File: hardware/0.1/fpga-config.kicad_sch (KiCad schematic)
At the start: 31 parts, among them J2 JTAG, J5 USB_C_Receptacle_USB2.0, Q1 BSS138, SW1 KMR2, U1 ECP5U_12_CABGA256, U4 USBLC6-2SC6, U6 W25Q128JVSIQ

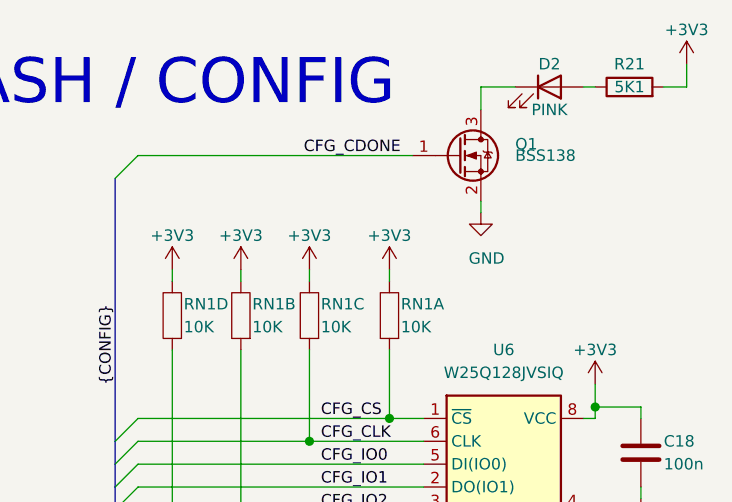
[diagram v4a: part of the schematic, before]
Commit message: change LEDs, optimise parts
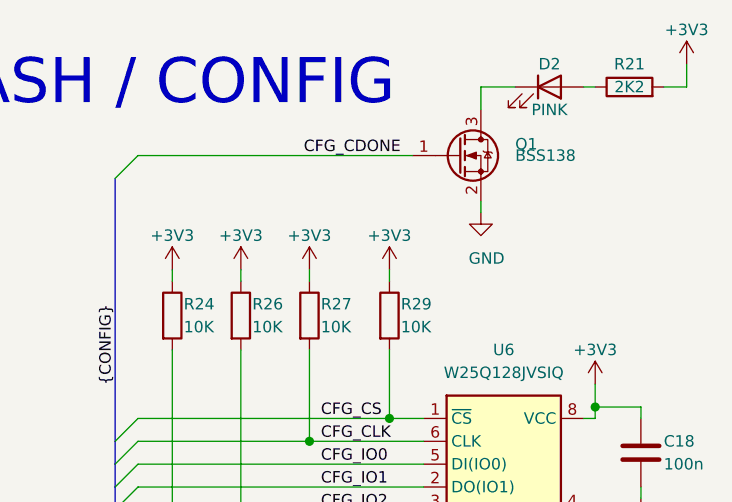
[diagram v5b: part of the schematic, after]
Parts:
- removed RN1: 10K, Resistor_SMD:R_Array_Convex_4x0402, symbol josh-passive:RN
- added R24, R26, R27, R29: 10K, Resistor_SMD:R_0402_1005Metric, symbol Device:R
- J5: footprint josh-connectors:USB_C_U262-161N-4BVC11 -> josh-connectors:USB_C_Receptacle_HRO_TYPE-C-31-M-12
- Q1: LCSC (none) -> C193366; MPN (none) -> BSS138PW,115
- R21: value 5K1 -> 2K2
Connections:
- net +3V3: now also R24.1, R26.1, R27.1, R29.1
- net CFG_CLK: now also R27.2
- net CFG_CS: now also R29.2
- net CFG_IO2: now also R26.2
- net CFG_IO3: now also R24.2
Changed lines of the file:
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@@
   (junction (at 269.24 57.15) (diameter 1.016) (color 0 0 0 0))
   (junction (at 269.24 71.12) (diameter 1.016) (color 0 0 0 0))
+  (no_connect (at 46.355 66.04))
+  (no_connect (at 229.87 137.16))
+  (no_connect (at 229.87 116.84))
+  (no_connect (at 229.87 111.76))
+  (no_connect (at 229.87 119.38))
+  (no_connect (at 229.87 144.78))
   (no_connect (at 229.87 121.92))
-  (no_connect (at 229.87 111.76))
-  (no_connect (at 229.87 144.78))
   (no_connect (at 46.355 63.5))
   (no_connect (at 229.87 114.3))
-  (no_connect (at 229.87 119.38))
-  (no_connect (at 229.87 116.84))
-  (no_connect (at 46.355 66.04))
-  (no_connect (at 229.87 137.16))
   (bus_entry (at 114.935 49.53) (size 2.54 -2.54)
     (stroke (width 0.1524) (type solid) (color 0 0 0 0))
@@
     (property "DNP" "" (id 4) (at 179.07 114.3 0)
       (effects (font (size 1.27 1.27)) (justify left bottom))
-    )
-  )
-  (symbol (lib_id "josh-passive:RN") (at 222.25 46.99 90) (unit 4)
-    (in_bom yes) (on_board yes)
-    (property "Reference" "RN1" (id 0) (at 223.52 45.72 90)
-      (effects (font (size 1.27 1.27)) (justify right))
-    )
-    (property "Value" "10K" (id 1) (at 223.52 48.26 90)
-      (effects (font (size 1.27 1.27)) (justify right))
-    )
-    (property "Footprint" "Resistor_SMD:R_Array_Convex_4x0402" (id 2) (at 222.25 46.99 90)
-      (effects (font (size 1.27 1.27)) hide)
-    )
-    (property "Datasheet" "~" (id 3) (at 222.25 46.99 90)
-      (effects (font (size 1.27 1.27)) hide)
-    )
-  )
-  (symbol (lib_id "josh-passive:RN") (at 229.87 46.99 90) (unit 2)
-    (in_bom yes) (on_board yes)
-    (property "Reference" "RN1" (id 0) (at 231.14 45.72 90)
-      (effects (font (size 1.27 1.27)) (justify right))
-    )
-    (property "Value" "10K" (id 1) (at 231.14 48.26 90)
-      (effects (font (size 1.27 1.27)) (justify right))
-    )
-    (property "Footprint" "Resistor_SMD:R_Array_Convex_4x0402" (id 2) (at 229.87 46.99 90)
-      (effects (font (size 1.27 1.27)) hide)
-    )
-    (property "Datasheet" "~" (id 3) (at 229.87 46.99 90)
-      (effects (font (size 1.27 1.27)) hide)
-    )
-  )
-  (symbol (lib_id "josh-passive:RN") (at 237.49 46.99 90) (unit 3)
-    (in_bom yes) (on_board yes)
-    (property "Reference" "RN1" (id 0) (at 238.76 45.72 90)
-      (effects (font (size 1.27 1.27)) (justify right))
-    )
-    (property "Value" "10K" (id 1) (at 238.76 48.26 90)
-      (effects (font (size 1.27 1.27)) (justify right))
-    )
-    (property "Footprint" "Resistor_SMD:R_Array_Convex_4x0402" (id 2) (at 237.49 46.99 90)
-      (effects (font (size 1.27 1.27)) hide)
-    )
-    (property "Datasheet" "~" (id 3) (at 237.49 46.99 90)
-      (effects (font (size 1.27 1.27)) hide)
-    )
-  )
-  (symbol (lib_id "josh-passive:RN") (at 246.38 46.99 90) (unit 1)
-    (in_bom yes) (on_board yes)
-    (property "Reference" "RN1" (id 0) (at 247.65 45.72 90)
-      (effects (font (size 1.27 1.27)) (justify right))
-    )
-    (property "Value" "10K" (id 1) (at 247.65 48.26 90)
-      (effects (font (size 1.27 1.27)) (justify right))
-    )
-    (property "Footprint" "Resistor_SMD:R_Array_Convex_4x0402" (id 2) (at 246.38 46.99 90)
-      (effects (font (size 1.27 1.27)) hide)
-    )
-    (property "Datasheet" "~" (id 3) (at 246.38 46.99 90)
-      (effects (font (size 1.27 1.27)) hide)
     )
   )
@@
     (property "DNP" "DNP" (id 4) (at 212.09 144.78 90))
   )
+  (symbol (lib_id "Device:R") (at 222.25 46.99 0) (unit 1)
+    (in_bom yes) (on_board yes)
+    (property "Reference" "R24" (id 0) (at 223.52 45.72 0)
+      (effects (font (size 1.27 1.27)) (justify left))
+    )
+    (property "Value" "10K" (id 1) (at 223.52 48.26 0)
+      (effects (font (size 1.27 1.27)) (justify left))
+    )
+    (property "Footprint" "Resistor_SMD:R_0402_1005Metric" (id 2) (at 220.472 46.99 90)
+      (effects (font (size 1.27 1.27)) hide)
+    )
+    (property "Datasheet" "~" (id 3) (at 222.25 46.99 0)
+      (effects (font (size 1.27 1.27)) hide)
+    )
+  )
+  (symbol (lib_id "Device:R") (at 229.87 46.99 0) (unit 1)
+    (in_bom yes) (on_board yes)
+    (property "Reference" "R26" (id 0) (at 231.14 45.72 0)
+      (effects (font (size 1.27 1.27)) (justify left))
+    )
+    (property "Value" "10K" (id 1) (at 231.14 48.26 0)
+      (effects (font (size 1.27 1.27)) (justify left))
+    )
+    (property "Footprint" "Resistor_SMD:R_0402_1005Metric" (id 2) (at 228.092 46.99 90)
+      (effects (font (size 1.27 1.27)) hide)
+    )
+    (property "Datasheet" "~" (id 3) (at 229.87 46.99 0)
+      (effects (font (size 1.27 1.27)) hide)
+    )
+  )
+  (symbol (lib_id "Device:R") (at 237.49 46.99 0) (unit 1)
+    (in_bom yes) (on_board yes)
+    (property "Reference" "R27" (id 0) (at 238.76 45.72 0)
+      (effects (font (size 1.27 1.27)) (justify left))
+    )
+    (property "Value" "10K" (id 1) (at 238.76 48.26 0)
+      (effects (font (size 1.27 1.27)) (justify left))
+    )
+    (property "Footprint" "Resistor_SMD:R_0402_1005Metric" (id 2) (at 235.712 46.99 90)
+      (effects (font (size 1.27 1.27)) hide)
+    )
+    (property "Datasheet" "~" (id 3) (at 237.49 46.99 0)
+      (effects (font (size 1.27 1.27)) hide)
+    )
+  )
+  (symbol (lib_id "Device:R") (at 246.38 46.99 0) (unit 1)
+    (in_bom yes) (on_board yes)
+    (property "Reference" "R29" (id 0) (at 247.65 45.72 0)
+      (effects (font (size 1.27 1.27)) (justify left))
+    )
+    (property "Value" "10K" (id 1) (at 247.65 48.26 0)
+      (effects (font (size 1.27 1.27)) (justify left))
+    )
+    (property "Footprint" "Resistor_SMD:R_0402_1005Metric" (id 2) (at 244.602 46.99 90)
+      (effects (font (size 1.27 1.27)) hide)
+    )
+    (property "Datasheet" "~" (id 3) (at 246.38 46.99 0)
+      (effects (font (size 1.27 1.27)) hide)
+    )
+  )
   (symbol (lib_id "Device:R") (at 273.05 21.59 90) (unit 1)
     (in_bom yes) (on_board yes)
     (property "Reference" "R21" (id 0) (at 273.05 19.05 90))
-    (property "Value" "5K1" (id 1) (at 273.05 21.59 90))
+    (property "Value" "2K2" (id 1) (at 273.05 21.59 90))
     (property "Footprint" "Resistor_SMD:R_0402_1005Metric" (id 2) (at 273.05 23.368 90)
       (effects (font (size 1.27 1.27)) hide)
@@
       (effects (font (size 1.27 1.27)) (justify left) hide)
     )
+    (property "LCSC" "C193366" (id 4) (at 254 29.21 0)
+      (effects (font (size 1.27 1.27)) hide)
+    )
+    (property "MPN" "BSS138PW,115" (id 5) (at 254 29.21 0)
+      (effects (font (size 1.27 1.27)) hide)
+    )
   )
   (symbol (lib_id "josh-ic:ECP5U_12_CABGA256") (at 78.74 104.14 0) (unit 9)
@@
     (property "Reference" "J5" (id 0) (at 22.225 29.21 0))
     (property "Value" "USB_C_Receptacle_USB2.0" (id 1) (at 33.655 31.75 0))
-    (property "Footprint" "josh-connectors:USB_C_U262-161N-4BVC11" (id 2) (at 34.925 50.8 0)
-      (effects (font (size 1.27 1.27)) hide)
-    )
+    (property "Footprint" "josh-connectors:USB_C_Receptacle_HRO_TYPE-C-31-M-12" (id 2) (at 34.925 50.8 0)
+      (effects (font (size 1.27 1.27)) hide)
+    )

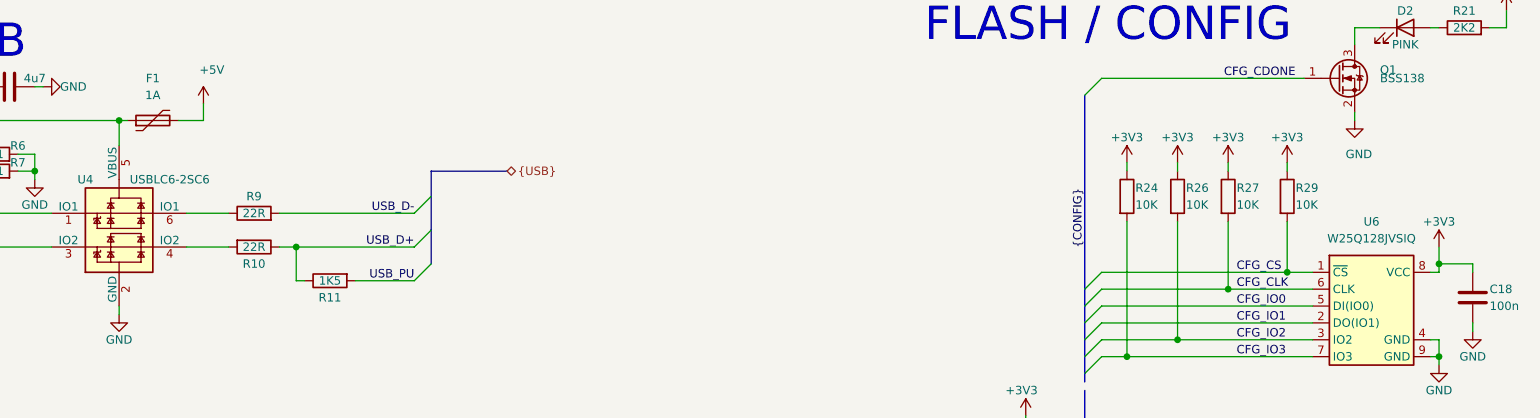
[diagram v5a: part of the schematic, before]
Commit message: add part numbers
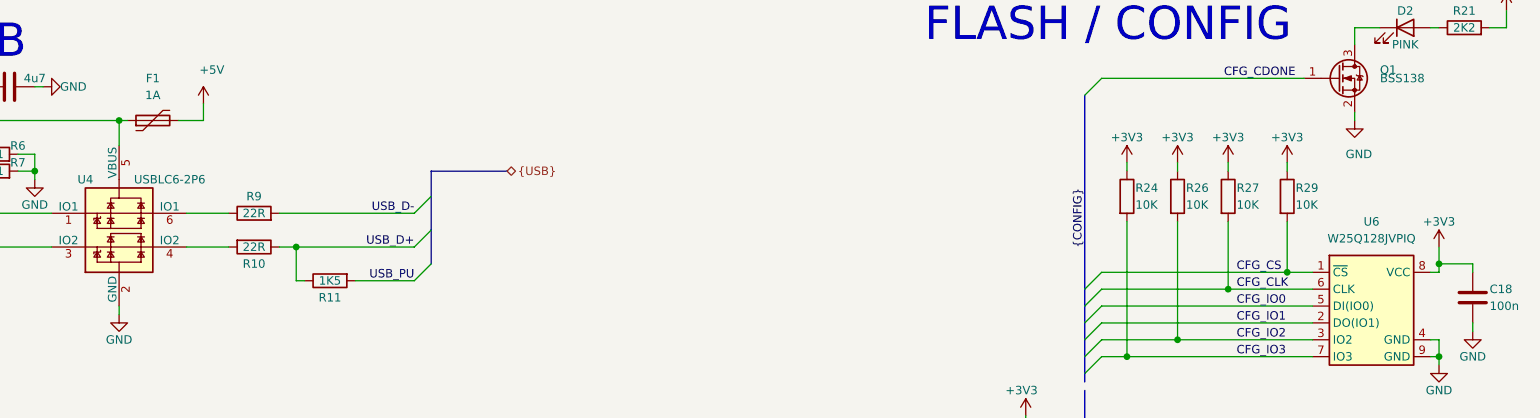
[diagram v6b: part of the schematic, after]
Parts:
- C13, C15, C17, C18: LCSC (none) -> C1525; MPN (none) -> CL05B104KO5NNNC; Manufacturer (none) -> Samsung Electro-Mechanics
- C6: LCSC (none) -> C19666; MPN (none) -> CL10A475KO8NNNC; Manufacturer (none) -> Samsung Electro-Mechanics
- D2: LCSC (none) -> C268294; MPN (none) -> OSK40603C1E; Manufacturer (none) -> OptoSupply
- F1: LCSC (none) -> C207017; MPN (none) -> 0603L100SLYR; Manufacturer (none) -> Littelfuse
- J5: LCSC (none) -> C165948; MPN (none) -> TYPE-C-31-M-12; Manufacturer (none) -> Korean Hroparts Elec
- Q1: Manufacturer (none) -> Nexperia
- R10, R20, R9: LCSC (none) -> C25152; MPN (none) -> 0402WGJ0220TCE; Manufacturer (none) -> UNI-ROYAL(Uniroyal Elec)
- R11, R13, R14, R15, R16, R17, R18: LCSC (none) -> C25867; MPN (none) -> 0402WGF1501TCE; Manufacturer (none) -> UNI-ROYAL(Uniroyal Elec)
- R12, R19, R6, R7: LCSC (none) -> C25905; MPN (none) -> 0402WGF5101TCE; Manufacturer (none) -> UNI-ROYAL(Uniroyal Elec)
- R21: LCSC (none) -> C25933; MPN (none) -> 0402WGJ0222TCE; Manufacturer (none) -> UNI-ROYAL(Uniroyal Elec)
- R24, R26, R27, R29, R8: LCSC (none) -> C25531; MPN (none) -> 0402WGJ0103TCE; Manufacturer (none) -> UNI-ROYAL(Uniroyal Elec)
- SW1: LCSC (none) -> C318893; MPN (none) -> TS-1185EC-C-D-B; Manufacturer (none) -> XKB Connectivity
- U1: MPN (none) -> LFE5U-12F-8BG256C; Manufacturer (none) -> Lattice; Mouser (none) -> 842-LFE5U12F8BG256C
- U4: value USBLC6-2SC6 -> USBLC6-2P6; LCSC (none) -> C15999; MPN (none) -> USBLC6-2P6; Manufacturer (none) -> STMicroelectronics
- U6: value W25Q128JVSIQ -> W25Q128JVPIQ; MPN (none) -> W25Q128JVPIM; Manufacturer (none) -> Winbond; Mouser (none) -> 454-W25Q128JVPIM

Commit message: design review done
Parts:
- U1: MPN LFE5U-12F-8BG256C -> LFE5U12F8BG256C
- U6: value W25Q128JVPIQ -> W25Q128JVPIM
